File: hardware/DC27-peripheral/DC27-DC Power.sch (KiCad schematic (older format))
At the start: 29 parts, among them J1 Conn_01x02_Male, J2 USB_B_Micro, U3 MIC2288, U4 MCP73811T-435I-OT, U5 PAM2305AAB120, U6 MAX17043

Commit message: commit the current hardware files
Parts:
- removed D34: SP0503BAHT, Package_TO_SOT_SMD:SOT-143, symbol Power_Protection:SP0503BAHT
- removed J2: USB_B_Micro, symbol Connector:USB_B_Micro
- added C24: 0.1uF, Capacitor_SMD:C_0603_1608Metric, symbol Device:C
- added J2: USB_MICRO_RIGHT, MF_Connectors:MF_Connectors-MICROUSB-RIGHT, symbol MF_Connectors:USB_MICRO_RIGHT
- added U8: TPD3E001DRLR, Package_TO_SOT_SMD:SOT-543, symbol Power_Protection:TPD3E001DRLR
- C10, C11, C12, C13, C14, C15, C16: footprint (none) -> Capacitor_SMD:C_0603_1608Metric
- D33, D35: footprint (none) -> Diode_SMD:D_SMA
- D36: footprint (none) -> LED_SMD:LED_0603_1608Metric
- F1: footprint (none) -> Fuse:Fuse_0603_1608Metric
- J1: footprint (none) -> Connector:JWT_A3963_1x02_P3.96mm_Vertical
- L1, L2: footprint (none) -> Inductor_SMD:L_0603_1608Metric
- R10, R11, R7, R8, R9: footprint (none) -> Resistor_SMD:R_0603_1608Metric
- TP1, TP3: footprint (none) -> TestPoint:TestPoint_Pad_D1.0mm
- TP2, TP4: footprint (none) -> TestPoint:TestPoint_2Pads_Pitch2.54mm_Drill0.8mm
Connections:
- wire segments 137 -> 139
- no-connect marks 2 -> 3
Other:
- note added: "ESD Protection\n"

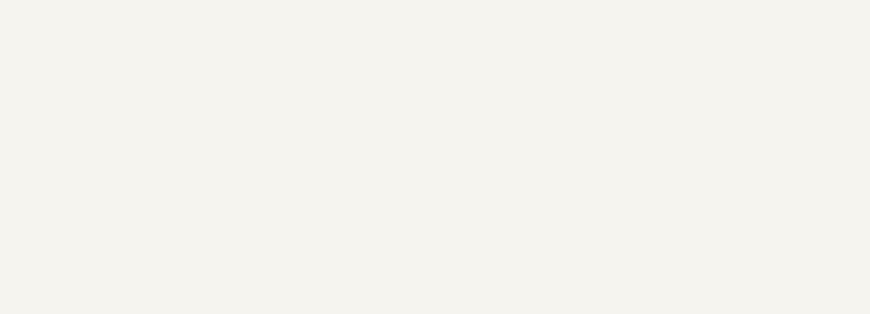
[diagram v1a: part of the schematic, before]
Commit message: Clean up SPI bus, set correct pins, start working through DRC errors.
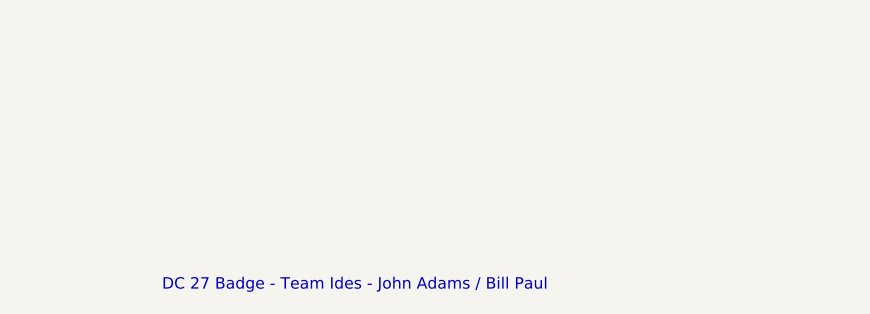
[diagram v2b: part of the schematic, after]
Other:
- note added: "DC 27 Badge - Team Ides - John Adams / Bill Paul"
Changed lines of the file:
@@
 Wire Wire Line
 	1250 3450 1250 3350
+Text Notes 7350 7500 0    50   ~ 0
+DC 27 Badge - Team Ides - John Adams / Bill Paul
 $EndSCHEMATC

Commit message: update badge schematic with new pins, verify every pin
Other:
- note added: "OPTIONAL Fuel Gauge Circuit\n"
- note removed: "Fuel Gauge Circuit\n"
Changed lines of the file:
@@
 	2750 6200 2750 6100
 Connection ~ 2400 6200
-Text Notes 750  4900 0    50   ~ 10
-Fuel Gauge Circuit\n
+Text Notes 600  4350 0    50   ~ 10
+OPTIONAL Fuel Gauge Circuit\n
 Wire Wire Line
 	1700 4650 1700 4750

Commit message: checkpoint all of the kicad stuff
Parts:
- added D36: CHARGE COMPLETE, LED_SMD:LED_0603_1608Metric, symbol Device:LED
- added R2: 330, Resistor_SMD:R_0603_1608Metric, symbol Device:R
- D35: renamed from D36; value LED -> USB POWER LED
- renumbered C24 to C14, C10 to C15, C11 to C16, C12 to C17, C13 to C18, C14 to C19, C15 to C20, C16 to C21, D35 to D34, J1 to J4, J2 to J5, R8 to R10, R9 to R11, R10 to R12, R11 to R13, R7 to R9, TP2 to TP10, TP3 to TP11, TP4 to TP12, TP1 to TP9, U8 to U4, U3 to U5, U4 to U6, U5 to U7, U6 to U8
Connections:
- net labels added: I2C_SCK, I2C_SDA
- net labels removed: SCL1, SDA1
- wire segments 139 -> 146

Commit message: checkpoint everything - schematic passing DRC
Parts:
- removed C14: 0.1uF, Capacitor_SMD:C_0603_1608Metric, symbol Device:C
- removed C15, C17, C18: 4.7uF, Capacitor_SMD:C_0603_1608Metric, symbol Device:C
- removed C16, C20: 22uF, Capacitor_SMD:C_0603_1608Metric, symbol Device:C
- removed C19: 10uF, Capacitor_SMD:C_0603_1608Metric, symbol Device:C
- removed D33, D34: MBRA140, Diode_SMD:D_SMA, symbol Device:D_Schottky
- removed D35: USB POWER LED, LED_SMD:LED_0603_1608Metric, symbol Device:LED
- removed D36: CHARGE COMPLETE, LED_SMD:LED_0603_1608Metric, symbol Device:LED
- removed F1: 1.1A, Fuse:Fuse_0603_1608Metric, symbol Device:Fuse_Small
- removed J4: Conn_01x02_Male, Connector:JWT_A3963_1x02_P3.96mm_Vertical, symbol Connector:Conn_01x02_Male
- removed J5: USB_MICRO_RIGHT, MF_Connectors:MF_Connectors-MICROUSB-RIGHT, symbol MF_Connectors:USB_MICRO_RIGHT
- removed L1, L2: 4.7uH, Inductor_SMD:L_0603_1608Metric, symbol Device:L
- removed R10: 1k87, Resistor_SMD:R_0603_1608Metric, symbol Device:R
- removed R11, R2: 330, Resistor_SMD:R_0603_1608Metric, symbol Device:R
- removed R12: 2.0k, Resistor_SMD:R_0603_1608Metric, symbol Device:R
- removed R9: 5k62, Resistor_SMD:R_0603_1608Metric, symbol Device:R
- removed TP10: 5v TEST, TestPoint:TestPoint_2Pads_Pitch2.54mm_Drill0.8mm, symbol Connector:TestPoint_2Pole
- removed TP11: VBATT, TestPoint:TestPoint_Pad_D1.0mm, symbol Connector:TestPoint
- removed TP12: 3.3V TEST, TestPoint:TestPoint_2Pads_Pitch2.54mm_Drill0.8mm, symbol Connector:TestPoint_2Pole
- removed TP9: VIN, TestPoint:TestPoint_Pad_D1.0mm, symbol Connector:TestPoint
- removed U4: TPD3E001DRLR, Package_TO_SOT_SMD:SOT-543, symbol Power_Protection:TPD3E001DRLR
- removed U5: MIC2288, Package_TO_SOT_SMD:SOT-23-5, symbol mic2288:MIC2288
- removed U6: MCP73811T-435I-OT, Package_TO_SOT_SMD:SOT-23-5, symbol Battery_Management:MCP73811T-435I-OT
- removed U7: PAM2305AAB120, Package_TO_SOT_SMD:TSOT-23-5, symbol Regulator_Switching:PAM2305AAB120
- added BT401: Battery, Connector_JST:JST_PH_S2B-PH-SM4-TB_1x02-1MP_P2.00mm_Horizontal, symbol Device:Battery
- added C401, C402, C403, C404, C405: 10uF, Capacitor_SMD:C_1206_3216Metric, symbol Device:C
- added C406: 1uF, Capacitor_SMD:C_1206_3216Metric, symbol Device:C
- added D401: CHG, Diode_SMD:D_0603_1608Metric, symbol Device:LED
- added D402: DONE, Diode_SMD:D_0603_1608Metric, symbol Device:LED
- added R401, R402: R, Resistor_SMD:R_0603_1608Metric, symbol Device:R
- added R403: 2.0k, Resistor_SMD:R_0603_1608Metric, symbol Device:R
- added SW401: POWER ON, Button_Switch_SMD:SW_SPDT_PCM12, symbol Switch:SW_SPDT
- added TP401: VBATT, TestPoint:TestPoint_Pad_D2.0mm, symbol Connector:TestPoint
- added TP402: 3.3V TEST, TestPoint:TestPoint_Pad_D2.0mm, symbol Connector:TestPoint
- added TP403: GND, TestPoint:TestPoint_Pad_D2.0mm, symbol Connector:TestPoint
- added U401: MCP73831-2-OT, Package_TO_SOT_SMD:SOT-23-5, symbol Battery_Management:MCP73831-2-OT
- added U402: LM1117-3.3, Package_TO_SOT_SMD:SOT-223, symbol Regulator_Linear:LM1117-3.3
- renumbered C21 to C407, R13 to R404, U8 to U403
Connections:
- net labels added: VBUS
- net labels removed: +5V, USBDATA+, USBDATA-, VCC3V3, VCC5V, VIN
- wire segments 146 -> 73
- no-connect marks 3 -> 2
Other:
- note added: "3.3v 650mA LDO\nPackage SOT-223"
- note added: "500MA LIPO CHARGER\nMCP73831"
- note added: "JST-PH MALE connector here \nPIN 1 (LEFT) HOT \n"
- note added: "MAX17043 i2c address 0x36\nCould send ALT to a interrupt pin for power down alerting\nPackage TDFN 8"
- note added: "VBUS is from USB\n"
- note removed: "DC/DC Supply +3v, +5v"
- note removed: "ESD Protection\n"
- note removed: "Expecting either +5 (VUSB) or \n3.7V (VBATT) here"
- note removed: "JST for Battery\n Pin 1 hot\n"
- note removed: "MAX17043 i2c address 0x36\nCould send ALT to a interrupt pin for power down alerting"
- note removed: "TODO: Do we even need the 5v supply?\n"
- note removed: "TODO:Maybe a bicolor LED here for charging/charged\n"
